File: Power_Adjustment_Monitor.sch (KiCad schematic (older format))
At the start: 23 parts, among them U10 LM317K, U7 LM337T, U8 LM317K, U9 LM337T

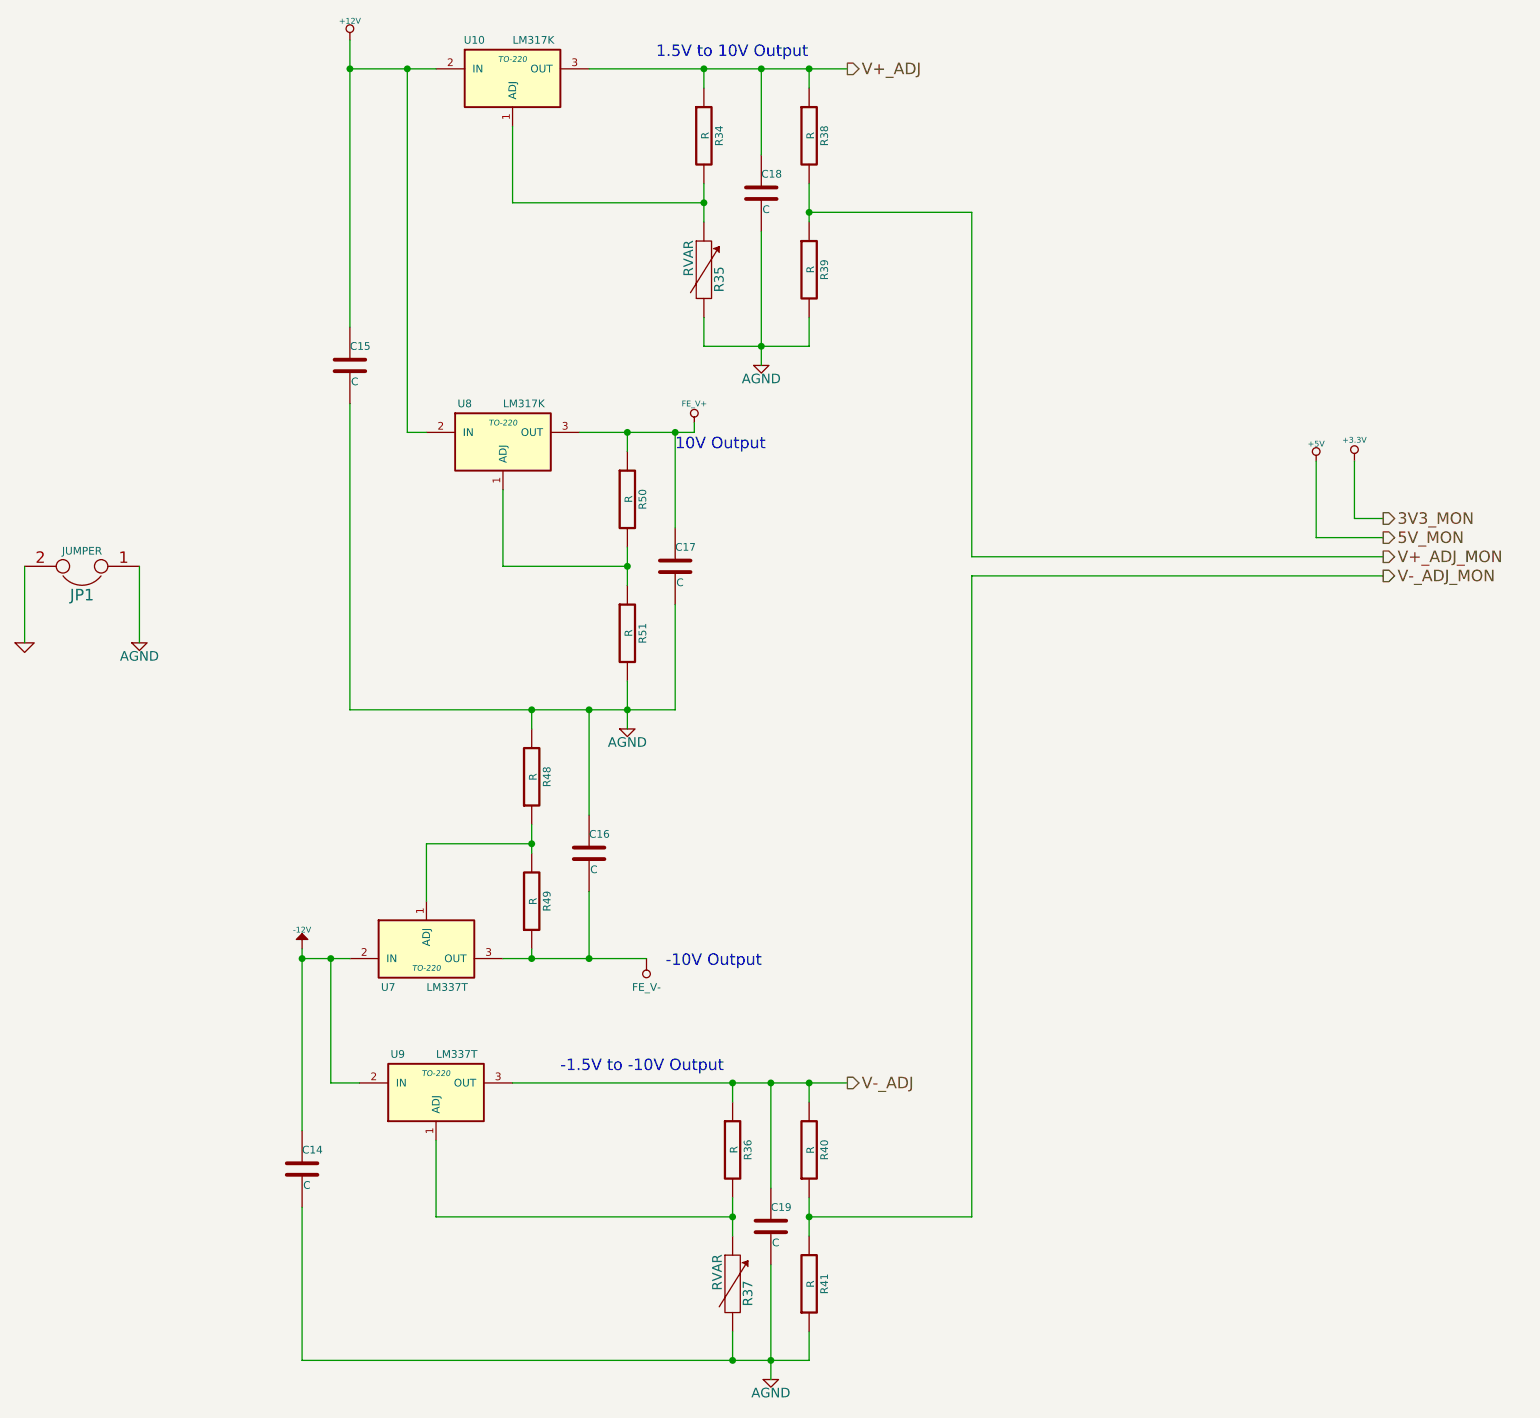
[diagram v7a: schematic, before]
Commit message: Layout v4.0
Adding ground planes according to location of modules
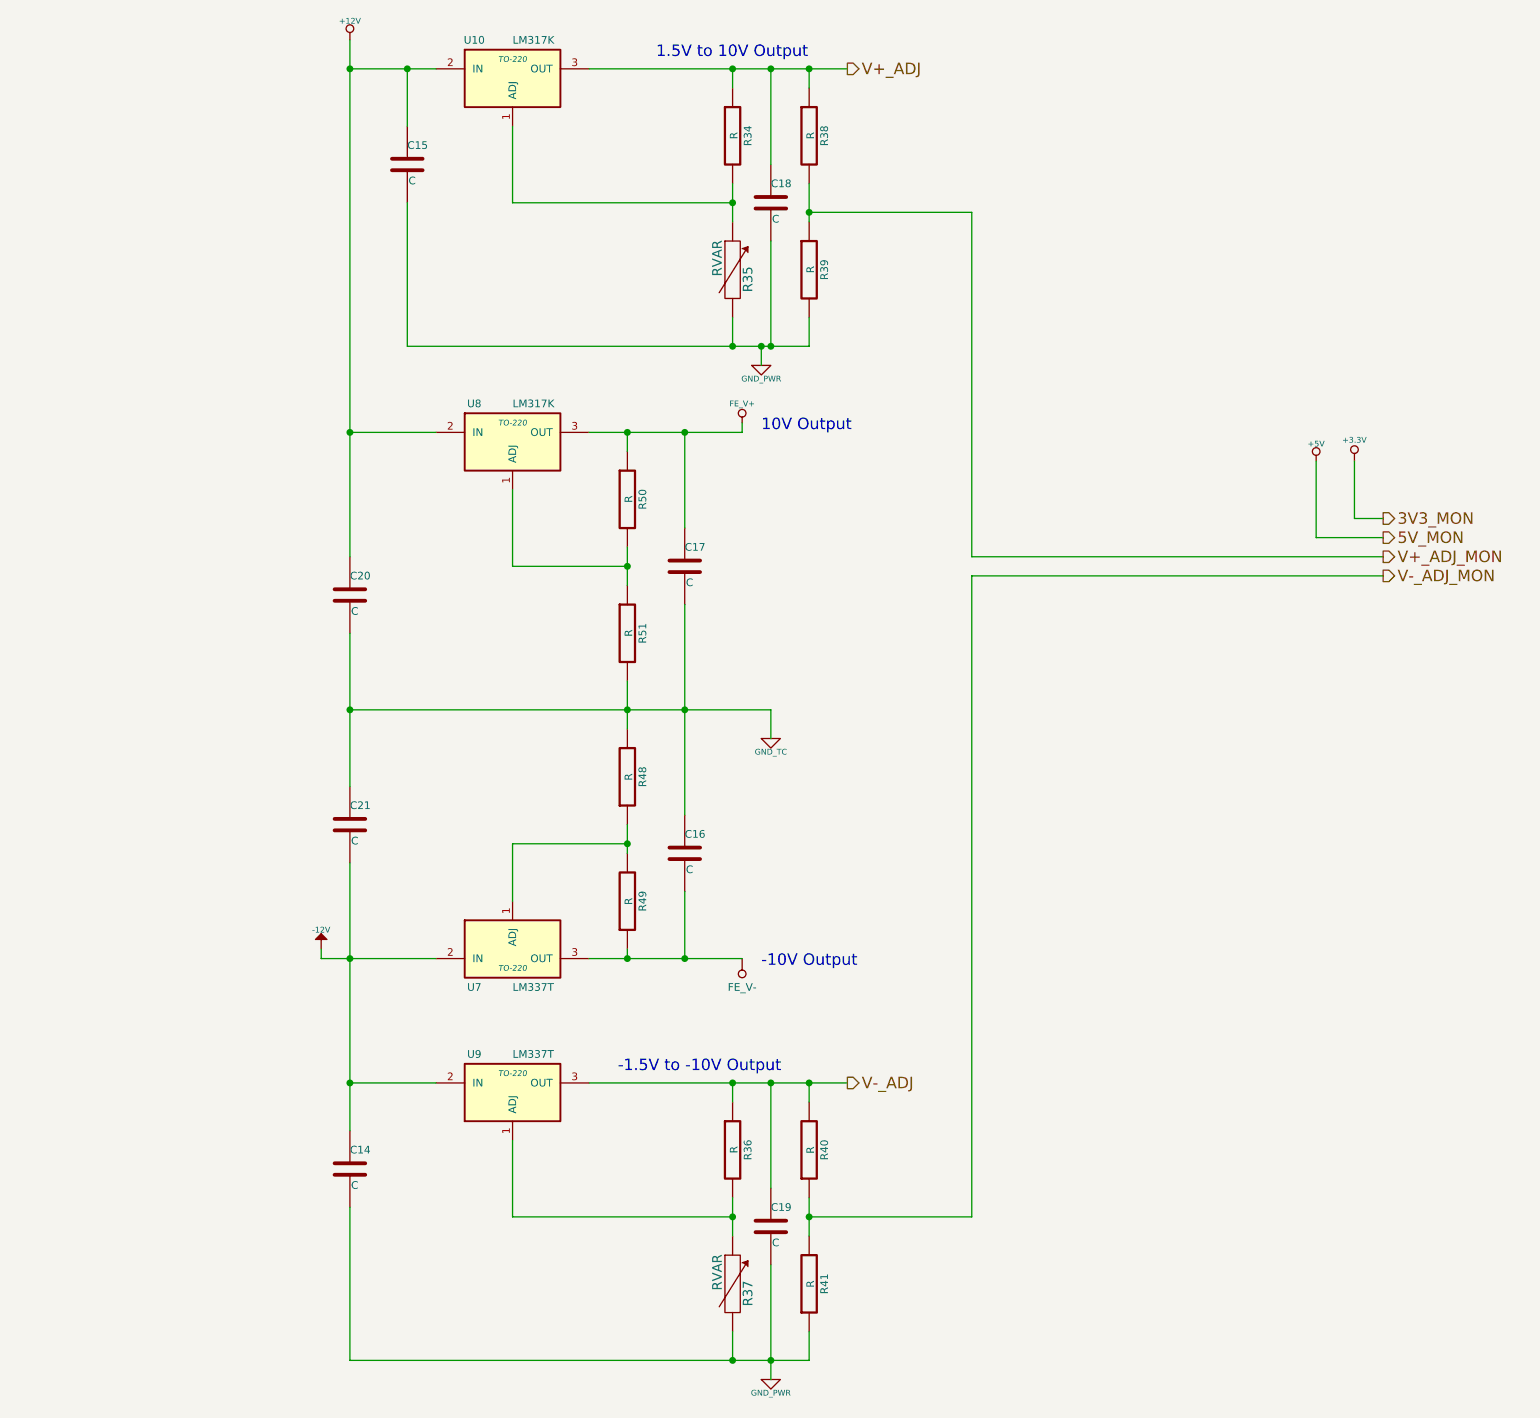
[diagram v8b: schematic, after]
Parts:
- removed JP1: JUMPER, ~, symbol JUMPER
- added C20, C21: C, ~, symbol C
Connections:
- net +12V: now also C20.1
- net -12V: now also C21.2
- net AGND renamed GND_PWR
- net GND_PWR: no longer C16.1, C17.2, R48.2, R51.2
- new net GND_TC: C16.1, C17.2, C20.2, C21.1, R48.2, R51.2
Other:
- moved on the sheet: C14, C15, C16, C17, C18, R34, R35, R48, R49, U7, U8, U9
